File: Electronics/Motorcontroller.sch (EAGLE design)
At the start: 39 parts, among them Q1 IRFZ48V, Q2 IRF4905V, Q3 IRFZ48V, Q4 IRF4905V, Q5 IRFZ48V, Q6 IRF4905V, Q7 IRFZ48V, Q8 IRF4905V, T1 BC547, T2 BC547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

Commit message: Reroute and tidy-up. New version number
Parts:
- R1, R2, R3: device rcl:R-EU_0207/10 -> rcl:R-EU_0207/7
- R4: device rcl:R-EU_0207/7 -> rcl:R-EU_0207/10
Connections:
- net +24V: now also R13.1; no longer LED1.A
- net GND2: now also LED1.C; no longer R13.1
- net N$6: now also LED1.A; no longer LED1.C
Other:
- moved on the sheet: LED1, R13
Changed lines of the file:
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@@
 <grid distance="0.1" unitdist="inch" unit="inch" style="lines" multiple="1" display="no" altdistance="0.01" altunitdist="inch" altunit="inch"/>
 <layers>
-<layer number="1" name="Top" color="4" fill="1" visible="no" active="no"/>
-<layer number="16" name="Bottom" color="1" fill="1" visible="no" active="no"/>
-<layer number="17" name="Pads" color="2" fill="1" visible="no" active="no"/>
-<layer number="18" name="Vias" color="2" fill="1" visible="no" active="no"/>
-<layer number="19" name="Unrouted" color="6" fill="1" visible="no" active="no"/>
-<layer number="20" name="Dimension" color="15" fill="1" visible="no" active="no"/>
-<layer number="21" name="tPlace" color="7" fill="1" visible="no" active="no"/>
-<layer number="22" name="bPlace" color="7" fill="1" visible="no" active="no"/>
-<layer number="23" name="tOrigins" color="15" fill="1" visible="no" active="no"/>
-<layer number="24" name="bOrigins" color="15" fill="1" visible="no" active="no"/>
-<layer number="25" name="tNames" color="7" fill="1" visible="no" active="no"/>
-<layer number="26" name="bNames" color="7" fill="1" visible="no" active="no"/>
-<layer number="27" name="tValues" color="7" fill="1" visible="no" active="no"/>
-<layer number="28" name="bValues" color="7" fill="1" visible="no" active="no"/>
+<layer number="1" name="Top" color="4" fill="1" visible="yes" active="no"/>
+<layer number="16" name="Bottom" color="1" fill="1" visible="yes" active="no"/>
+<layer number="17" name="Pads" color="2" fill="1" visible="yes" active="no"/>
+<layer number="18" name="Vias" color="2" fill="1" visible="yes" active="no"/>
+<layer number="19" name="Unrouted" color="6" fill="1" visible="yes" active="no"/>
+<layer number="20" name="Dimension" color="15" fill="1" visible="yes" active="no"/>
+<layer number="21" name="tPlace" color="7" fill="1" visible="yes" active="no"/>
+<layer number="22" name="bPlace" color="7" fill="1" visible="yes" active="no"/>
+<layer number="23" name="tOrigins" color="15" fill="1" visible="yes" active="no"/>
+<layer number="24" name="bOrigins" color="15" fill="1" visible="yes" active="no"/>
+<layer number="25" name="tNames" color="7" fill="1" visible="yes" active="no"/>
+<layer number="26" name="bNames" color="7" fill="1" visible="yes" active="no"/>
+<layer number="27" name="tValues" color="7" fill="1" visible="yes" active="no"/>
+<layer number="28" name="bValues" color="7" fill="1" visible="yes" active="no"/>
 <layer number="29" name="tStop" color="7" fill="3" visible="no" active="no"/>
 <layer number="30" name="bStop" color="7" fill="6" visible="no" active="no"/>
@@
 <layer number="35" name="tGlue" color="7" fill="4" visible="no" active="no"/>
 <layer number="36" name="bGlue" color="7" fill="5" visible="no" active="no"/>
-<layer number="37" name="tTest" color="7" fill="1" visible="no" active="no"/>
-<layer number="38" name="bTest" color="7" fill="1" visible="no" active="no"/>
+<layer number="37" name="tTest" color="7" fill="1" visible="yes" active="no"/>
+<layer number="38" name="bTest" color="7" fill="1" visible="yes" active="no"/>
 <layer number="39" name="tKeepout" color="4" fill="11" visible="no" active="no"/>
 <layer number="40" name="bKeepout" color="1" fill="11" visible="no" active="no"/>
@@
 <layer number="44" name="Drills" color="7" fill="1" visible="no" active="no"/>
 <layer number="45" name="Holes" color="7" fill="1" visible="no" active="no"/>
-<layer number="46" name="Milling" color="3" fill="1" visible="no" active="no"/>
-<layer number="47" name="Measures" color="7" fill="1" visible="no" active="no"/>
-<layer number="48" name="Document" color="7" fill="1" visible="no" active="no"/>
-<layer number="49" name="Reference" color="7" fill="1" visible="no" active="no"/>
-<layer number="50" name="dxf" color="7" fill="1" visible="no" active="no"/>
-<layer number="51" name="tDocu" color="7" fill="1" visible="no" active="no"/>
-<layer number="52" name="bDocu" color="7" fill="1" visible="no" active="no"/>
-<layer number="53" name="tGND_GNDA" color="7" fill="9" visible="no" active="no"/>
-<layer number="54" name="bGND_GNDA" color="1" fill="9" visible="no" active="no"/>
-<layer number="56" name="wert" color="7" fill="1" visible="no" active="no"/>
+<layer number="46" name="Milling" color="3" fill="1" visible="yes" active="no"/>
+<layer number="47" name="Measures" color="7" fill="1" visible="yes" active="no"/>
+<layer number="48" name="Document" color="7" fill="1" visible="yes" active="no"/>
+<layer number="49" name="Reference" color="7" fill="1" visible="yes" active="no"/>
+<layer number="50" name="dxf" color="7" fill="1" visible="yes" active="no"/>
+<layer number="51" name="tDocu" color="7" fill="1" visible="yes" active="no"/>
+<layer number="52" name="bDocu" color="7" fill="1" visible="yes" active="no"/>
+<layer number="53" name="tGND_GNDA" color="7" fill="9" visible="yes" active="no"/>
+<layer number="54" name="bGND_GNDA" color="1" fill="9" visible="yes" active="no"/>
+<layer number="56" name="wert" color="7" fill="1" visible="yes" active="no"/>
 <layer number="91" name="Nets" color="2" fill="1" visible="yes" active="yes"/>
 <layer number="92" name="Busses" color="1" fill="1" visible="yes" active="yes"/>
@@
 <part name="Q1" library="transistor-power" deviceset="IRFZ48" device="V"/>
 <part name="Q2" library="transistor-power" deviceset="IRF4905" device="V"/>
-<part name="R1" library="rcl" deviceset="R-EU_" device="0207/10" value="10k"/>
-<part name="R2" library="rcl" deviceset="R-EU_" device="0207/10" value="10k"/>
-<part name="R3" library="rcl" deviceset="R-EU_" device="0207/10" value="10k"/>
+<part name="R1" library="rcl" deviceset="R-EU_" device="0207/7" value="10k"/>
+<part name="R2" library="rcl" deviceset="R-EU_" device="0207/7" value="10k"/>
+<part name="R3" library="rcl" deviceset="R-EU_" device="0207/7" value="10k"/>
 <part name="Q7" library="transistor-power" deviceset="IRFZ48" device="V"/>
 <part name="Q8" library="transistor-power" deviceset="IRF4905" device="V"/>
@@
 <part name="Q5" library="transistor-power" deviceset="IRFZ48" device="V"/>
 <part name="Q6" library="transistor-power" deviceset="IRF4905" device="V"/>
-<part name="R4" library="rcl" deviceset="R-EU_" device="0207/7" value="10k"/>
+<part name="R4" library="rcl" deviceset="R-EU_" device="0207/10" value="10k"/>
 <part name="R5" library="rcl" deviceset="R-EU_" device="0207/10" value="10k"/>
 <part name="R6" library="rcl" deviceset="R-EU_" device="0207/10" value="10k"/>
@@
 <instance part="P+1" gate="1" x="203.2" y="170.18"/>
 <instance part="P+5" gate="1" x="175.26" y="144.78"/>
-<instance part="R13" gate="G$1" x="210.82" y="154.94" rot="R90"/>
-<instance part="LED1" gate="G$1" x="210.82" y="165.1"/>
+<instance part="R13" gate="G$1" x="210.82" y="162.56" rot="R270"/>
+<instance part="LED1" gate="G$1" x="210.82" y="154.94"/>
 <instance part="OK1" gate="G$1" x="165.1" y="127"/>
 <instance part="OK2" gate="G$1" x="165.1" y="111.76"/>
@@
 <wire x1="195.58" y1="154.94" x2="195.58" y2="149.86" width="0.1524" layer="91"/>
 <wire x1="195.58" y1="149.86" x2="193.04" y2="149.86" width="0.1524" layer="91"/>
-<pinref part="R13" gate="G$1" pin="1"/>
-<junction x="203.2" y="149.86"/>
 <junction x="195.58" y="149.86"/>
 <pinref part="C1" gate="G$1" pin="-"/>
+<pinref part="LED1" gate="G$1" pin="C"/>
 <wire x1="203.2" y1="149.86" x2="210.82" y2="149.86" width="0.1524" layer="91"/>
+<junction x="203.2" y="149.86"/>
 </segment>
 <segment>
@@
 <pinref part="X3" gate="-1" pin="KL"/>
 <wire x1="195.58" y1="167.64" x2="203.2" y2="167.64" width="0.1524" layer="91"/>
-<pinref part="LED1" gate="G$1" pin="A"/>
-<junction x="203.2" y="167.64"/>
 <pinref part="C1" gate="G$1" pin="+"/>
 <wire x1="195.58" y1="162.56" x2="195.58" y2="167.64" width="0.1524" layer="91"/>
 <junction x="195.58" y="167.64"/>
-<wire x1="203.2" y1="167.64" x2="210.82" y2="167.64" width="0.1524" layer="91"/>
+<pinref part="R13" gate="G$1" pin="1"/>
+<wire x1="210.82" y1="167.64" x2="203.2" y2="167.64" width="0.1524" layer="91"/>
+<junction x="203.2" y="167.64"/>
 </segment>
 <segment>
@@
 </segment>
 </net>
-<net name="N$6" class="0">
-<segment>
-<pinref part="R13" gate="G$1" pin="2"/>
-<pinref part="LED1" gate="G$1" pin="C"/>
-</segment>
-</net>
 <net name="N$3" class="0">
 <segment>
@@
 </segment>
 </net>
+<net name="N$6" class="0">
+<segment>
+<pinref part="LED1" gate="G$1" pin="A"/>
+<pinref part="R13" gate="G$1" pin="2"/>
+</segment>
+</net>

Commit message: Fixed airwire in motorboard. Updated .pdf and rapport
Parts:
- R3: device rcl:R-EU_0207/7 -> rcl:R-EU_0207/10
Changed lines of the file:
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@@
 <?xml version="1.0" encoding="utf-8"?>
 <!DOCTYPE eagle SYSTEM "eagle.dtd">
-<eagle version="6.1">
+<eagle version="6.2">
 <drawing>
 <settings>
@@
 <part name="R1" library="rcl" deviceset="R-EU_" device="0207/7" value="10k"/>
 <part name="R2" library="rcl" deviceset="R-EU_" device="0207/7" value="10k"/>
-<part name="R3" library="rcl" deviceset="R-EU_" device="0207/7" value="10k"/>
+<part name="R3" library="rcl" deviceset="R-EU_" device="0207/10" value="10k"/>
 <part name="Q7" library="transistor-power" deviceset="IRFZ48" device="V"/>
 <part name="Q8" library="transistor-power" deviceset="IRF4905" device="V"/>

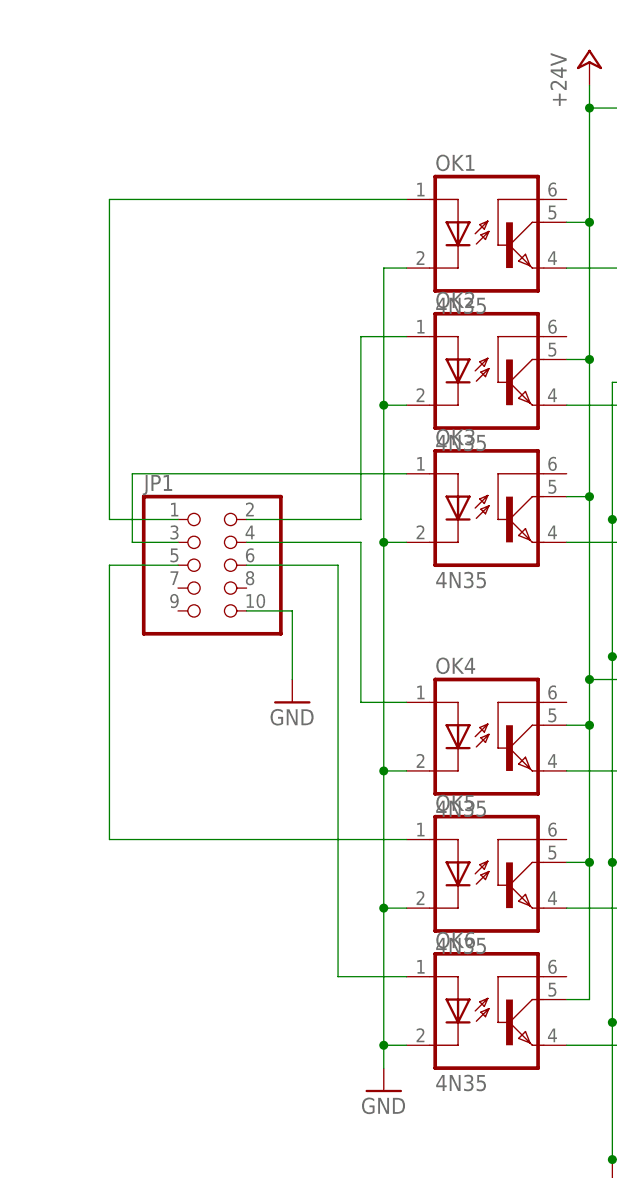
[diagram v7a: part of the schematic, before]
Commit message: Moved resistors to Motorboard. Closes #37
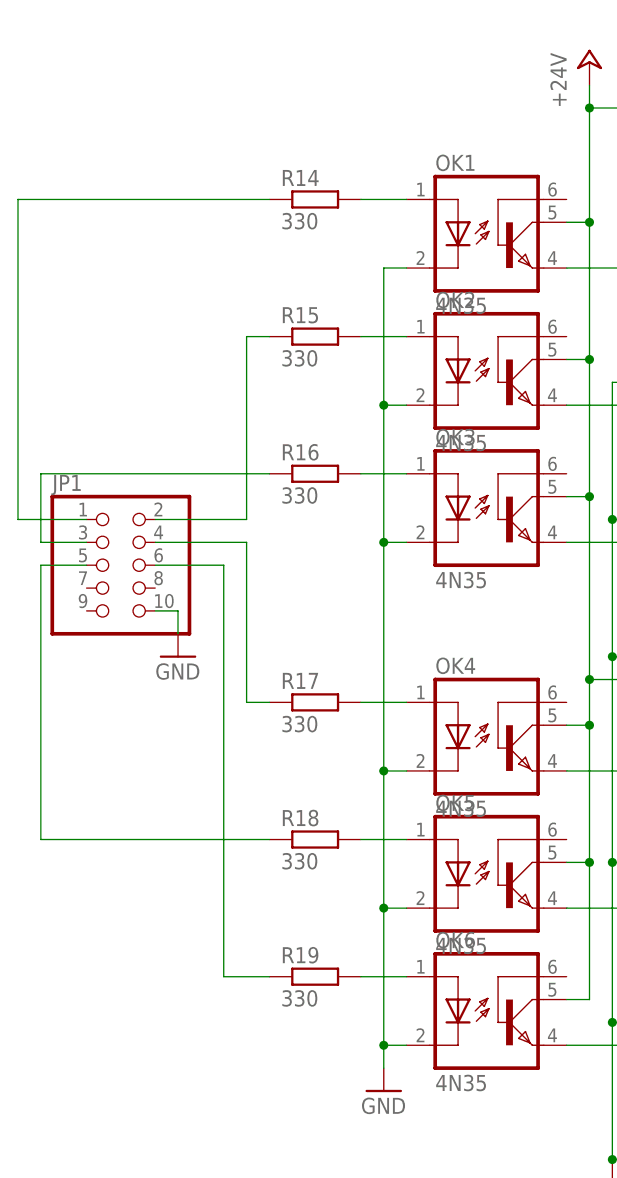
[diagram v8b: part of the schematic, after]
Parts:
- added R14, R15, R16, R17, R18, R19: 330, rcl:R-EU_0207/7
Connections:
- new net N$29: OK1.A, R14.2
- new net N$30: OK2.A, R15.2
- new net N$31: OK3.A, R16.2
- new net N$32: OK4.A, R17.2
- new net N$36: OK5.A, R18.2
- new net N$37: OK6.A, R19.2
- net N$10: now also R18.1; no longer OK5.A
- net N$11: now also R19.1; no longer OK6.A
- net N$3: now also R14.1; no longer OK1.A
- net N$5: now also R15.1; no longer OK2.A
- net N$7: now also R16.1; no longer OK3.A
- net N$8: now also R17.1; no longer OK4.A
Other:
- moved on the sheet: JP1
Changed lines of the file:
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@@
 <part name="T2" library="transistor" deviceset="BC547" device=""/>
 <part name="R12" library="rcl" deviceset="R-EU_" device="0207/10" value="10k"/>
+<part name="R14" library="rcl" deviceset="R-EU_" device="0207/7" value="330"/>
+<part name="R15" library="rcl" deviceset="R-EU_" device="0207/7" value="330"/>
+<part name="R16" library="rcl" deviceset="R-EU_" device="0207/7" value="330"/>
+<part name="R17" library="rcl" deviceset="R-EU_" device="0207/7" value="330"/>
+<part name="R18" library="rcl" deviceset="R-EU_" device="0207/7" value="330"/>
+<part name="R19" library="rcl" deviceset="R-EU_" device="0207/7" value="330"/>
 </parts>
 <sheets>
@@
 <instance part="OK5" gate="G$1" x="165.1" y="55.88"/>
 <instance part="OK6" gate="G$1" x="165.1" y="40.64"/>
-<instance part="JP1" gate="A" x="132.08" y="88.9"/>
-<instance part="GND1" gate="1" x="142.24" y="73.66"/>
+<instance part="JP1" gate="A" x="121.92" y="88.9"/>
+<instance part="GND1" gate="1" x="129.54" y="78.74"/>
 <instance part="C1" gate="G$1" x="195.58" y="160.02"/>
 <instance part="LED2" gate="G$1" x="248.92" y="124.46"/>
@@
 <instance part="T2" gate="G$1" x="218.44" y="58.42"/>
 <instance part="R12" gate="G$1" x="220.98" y="71.12" rot="R90"/>
+<instance part="R14" gate="G$1" x="144.78" y="129.54"/>
+<instance part="R15" gate="G$1" x="144.78" y="114.3"/>
+<instance part="R16" gate="G$1" x="144.78" y="99.06"/>
+<instance part="R17" gate="G$1" x="144.78" y="73.66"/>
+<instance part="R18" gate="G$1" x="144.78" y="58.42"/>
+<instance part="R19" gate="G$1" x="144.78" y="43.18"/>
 </instances>
 <busses>
@@
 <pinref part="JP1" gate="A" pin="10"/>
 <pinref part="GND1" gate="1" pin="GND"/>
-<wire x1="137.16" y1="83.82" x2="142.24" y2="83.82" width="0.1524" layer="91"/>
-<wire x1="142.24" y1="83.82" x2="142.24" y2="76.2" width="0.1524" layer="91"/>
+<wire x1="127" y1="83.82" x2="129.54" y2="83.82" width="0.1524" layer="91"/>
+<wire x1="129.54" y1="83.82" x2="129.54" y2="81.28" width="0.1524" layer="91"/>
 </segment>
 </net>
@@
 <net name="N$3" class="0">
 <segment>
-<pinref part="OK1" gate="G$1" pin="A"/>
-<wire x1="154.94" y1="129.54" x2="121.92" y2="129.54" width="0.1524" layer="91"/>
-<wire x1="121.92" y1="129.54" x2="121.92" y2="93.98" width="0.1524" layer="91"/>
+<wire x1="111.76" y1="129.54" x2="111.76" y2="93.98" width="0.1524" layer="91"/>
 <pinref part="JP1" gate="A" pin="1"/>
-<wire x1="121.92" y1="93.98" x2="129.54" y2="93.98" width="0.1524" layer="91"/>
-</segment>
-</net>
-<net name="N$5" class="0">
-<segment>
-<pinref part="OK2" gate="G$1" pin="A"/>
-<wire x1="154.94" y1="114.3" x2="149.86" y2="114.3" width="0.1524" layer="91"/>
-<wire x1="149.86" y1="114.3" x2="149.86" y2="93.98" width="0.1524" layer="91"/>
-<pinref part="JP1" gate="A" pin="2"/>
-<wire x1="149.86" y1="93.98" x2="137.16" y2="93.98" width="0.1524" layer="91"/>
+<wire x1="111.76" y1="93.98" x2="119.38" y2="93.98" width="0.1524" layer="91"/>
+<pinref part="R14" gate="G$1" pin="1"/>
+<wire x1="139.7" y1="129.54" x2="111.76" y2="129.54" width="0.1524" layer="91"/>
 </segment>
 </net>
 <net name="N$7" class="0">
 <segment>
-<pinref part="OK3" gate="G$1" pin="A"/>
-<wire x1="154.94" y1="99.06" x2="124.46" y2="99.06" width="0.1524" layer="91"/>
-<wire x1="124.46" y1="99.06" x2="124.46" y2="91.44" width="0.1524" layer="91"/>
+<wire x1="114.3" y1="99.06" x2="114.3" y2="91.44" width="0.1524" layer="91"/>
 <pinref part="JP1" gate="A" pin="3"/>
-<wire x1="124.46" y1="91.44" x2="129.54" y2="91.44" width="0.1524" layer="91"/>
+<wire x1="114.3" y1="91.44" x2="119.38" y2="91.44" width="0.1524" layer="91"/>
+<pinref part="R16" gate="G$1" pin="1"/>
+<wire x1="139.7" y1="99.06" x2="114.3" y2="99.06" width="0.1524" layer="91"/>
 </segment>
 </net>
 <net name="N$8" class="0">
 <segment>
-<wire x1="149.86" y1="73.66" x2="149.86" y2="91.44" width="0.1524" layer="91"/>
 <pinref part="JP1" gate="A" pin="4"/>
-<wire x1="149.86" y1="91.44" x2="137.16" y2="91.44" width="0.1524" layer="91"/>
-<pinref part="OK4" gate="G$1" pin="A"/>
-<wire x1="154.94" y1="73.66" x2="149.86" y2="73.66" width="0.1524" layer="91"/>
+<pinref part="R17" gate="G$1" pin="1"/>
+<wire x1="137.16" y1="91.44" x2="127" y2="91.44" width="0.1524" layer="91"/>
+<wire x1="139.7" y1="73.66" x2="137.16" y2="73.66" width="0.1524" layer="91"/>
+<wire x1="137.16" y1="73.66" x2="137.16" y2="91.44" width="0.1524" layer="91"/>
 </segment>
 </net>
 <net name="N$10" class="0">
 <segment>
-<wire x1="121.92" y1="58.42" x2="121.92" y2="88.9" width="0.1524" layer="91"/>
+<wire x1="114.3" y1="58.42" x2="114.3" y2="88.9" width="0.1524" layer="91"/>
 <pinref part="JP1" gate="A" pin="5"/>
-<wire x1="121.92" y1="88.9" x2="129.54" y2="88.9" width="0.1524" layer="91"/>
-<pinref part="OK5" gate="G$1" pin="A"/>
-<wire x1="154.94" y1="58.42" x2="121.92" y2="58.42" width="0.1524" layer="91"/>
+<wire x1="114.3" y1="88.9" x2="119.38" y2="88.9" width="0.1524" layer="91"/>
+<pinref part="R18" gate="G$1" pin="1"/>
+<wire x1="114.3" y1="58.42" x2="139.7" y2="58.42" width="0.1524" layer="91"/>
 </segment>
 </net>
 <net name="N$11" class="0">
 <segment>
-<pinref part="OK6" gate="G$1" pin="A"/>
-<wire x1="154.94" y1="43.18" x2="147.32" y2="43.18" width="0.1524" layer="91"/>
-<wire x1="147.32" y1="43.18" x2="147.32" y2="88.9" width="0.1524" layer="91"/>
+<wire x1="134.62" y1="43.18" x2="134.62" y2="88.9" width="0.1524" layer="91"/>
 <pinref part="JP1" gate="A" pin="6"/>
-<wire x1="147.32" y1="88.9" x2="137.16" y2="88.9" width="0.1524" layer="91"/>
+<wire x1="134.62" y1="88.9" x2="127" y2="88.9" width="0.1524" layer="91"/>
+<pinref part="R19" gate="G$1" pin="1"/>
+<wire x1="139.7" y1="43.18" x2="134.62" y2="43.18" width="0.1524" layer="91"/>
 </segment>
 </net>
@@
 </segment>
 </net>
+<net name="N$5" class="0">
+<segment>
+<pinref part="R15" gate="G$1" pin="1"/>
+<wire x1="137.16" y1="114.3" x2="139.7" y2="114.3" width="0.1524" layer="91"/>
+<wire x1="137.16" y1="114.3" x2="137.16" y2="93.98" width="0.1524" layer="91"/>
+<pinref part="JP1" gate="A" pin="2"/>
+<wire x1="137.16" y1="93.98" x2="127" y2="93.98" width="0.1524" layer="91"/>
+</segment>
+</net>
+<net name="N$29" class="0">
+<segment>
+<pinref part="R14" gate="G$1" pin="2"/>
+<pinref part="OK1" gate="G$1" pin="A"/>
+<wire x1="149.86" y1="129.54" x2="154.94" y2="129.54" width="0.1524" layer="91"/>
+</segment>
+</net>
+<net name="N$30" class="0">
+<segment>
+<pinref part="R15" gate="G$1" pin="2"/>
+<pinref part="OK2" gate="G$1" pin="A"/>
+<wire x1="149.86" y1="114.3" x2="154.94" y2="114.3" width="0.1524" layer="91"/>
+</segment>
+</net>
+<net name="N$31" class="0">
+<segment>
+<pinref part="R16" gate="G$1" pin="2"/>
+<pinref part="OK3" gate="G$1" pin="A"/>
+<wire x1="149.86" y1="99.06" x2="154.94" y2="99.06" width="0.1524" layer="91"/>
+</segment>
+</net>
+<net name="N$32" class="0">
+<segment>
+<pinref part="R17" gate="G$1" pin="2"/>
+<pinref part="OK4" gate="G$1" pin="A"/>
+<wire x1="149.86" y1="73.66" x2="154.94" y2="73.66" width="0.1524" layer="91"/>
+</segment>
+</net>
+<net name="N$36" class="0">
+<segment>
+<pinref part="R18" gate="G$1" pin="2"/>
+<pinref part="OK5" gate="G$1" pin="A"/>
+<wire x1="149.86" y1="58.42" x2="154.94" y2="58.42" width="0.1524" layer="91"/>
+</segment>
+</net>
+<net name="N$37" class="0">
+<segment>
+<pinref part="R19" gate="G$1" pin="2"/>
+<pinref part="OK6" gate="G$1" pin="A"/>
+<wire x1="149.86" y1="43.18" x2="154.94" y2="43.18" width="0.1524" layer="91"/>
+</segment>
+</net>
